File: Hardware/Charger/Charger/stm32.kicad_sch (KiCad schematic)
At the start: 48 parts, among them J5 Conn_01x04_Socket, J6 Conn_01x04, J7 Conn_02x03_Counter_Clockwise, SW1 SW_Push, SW2 SW_Push, SW3 SW_Push, SW4 SW_Push, SW5 SW_Push, SW6 SW_Push, U3 TCAN1042VDRQ1, U4 STM32G473CCTx, U5 LTV-356T, Y1 48 MHz

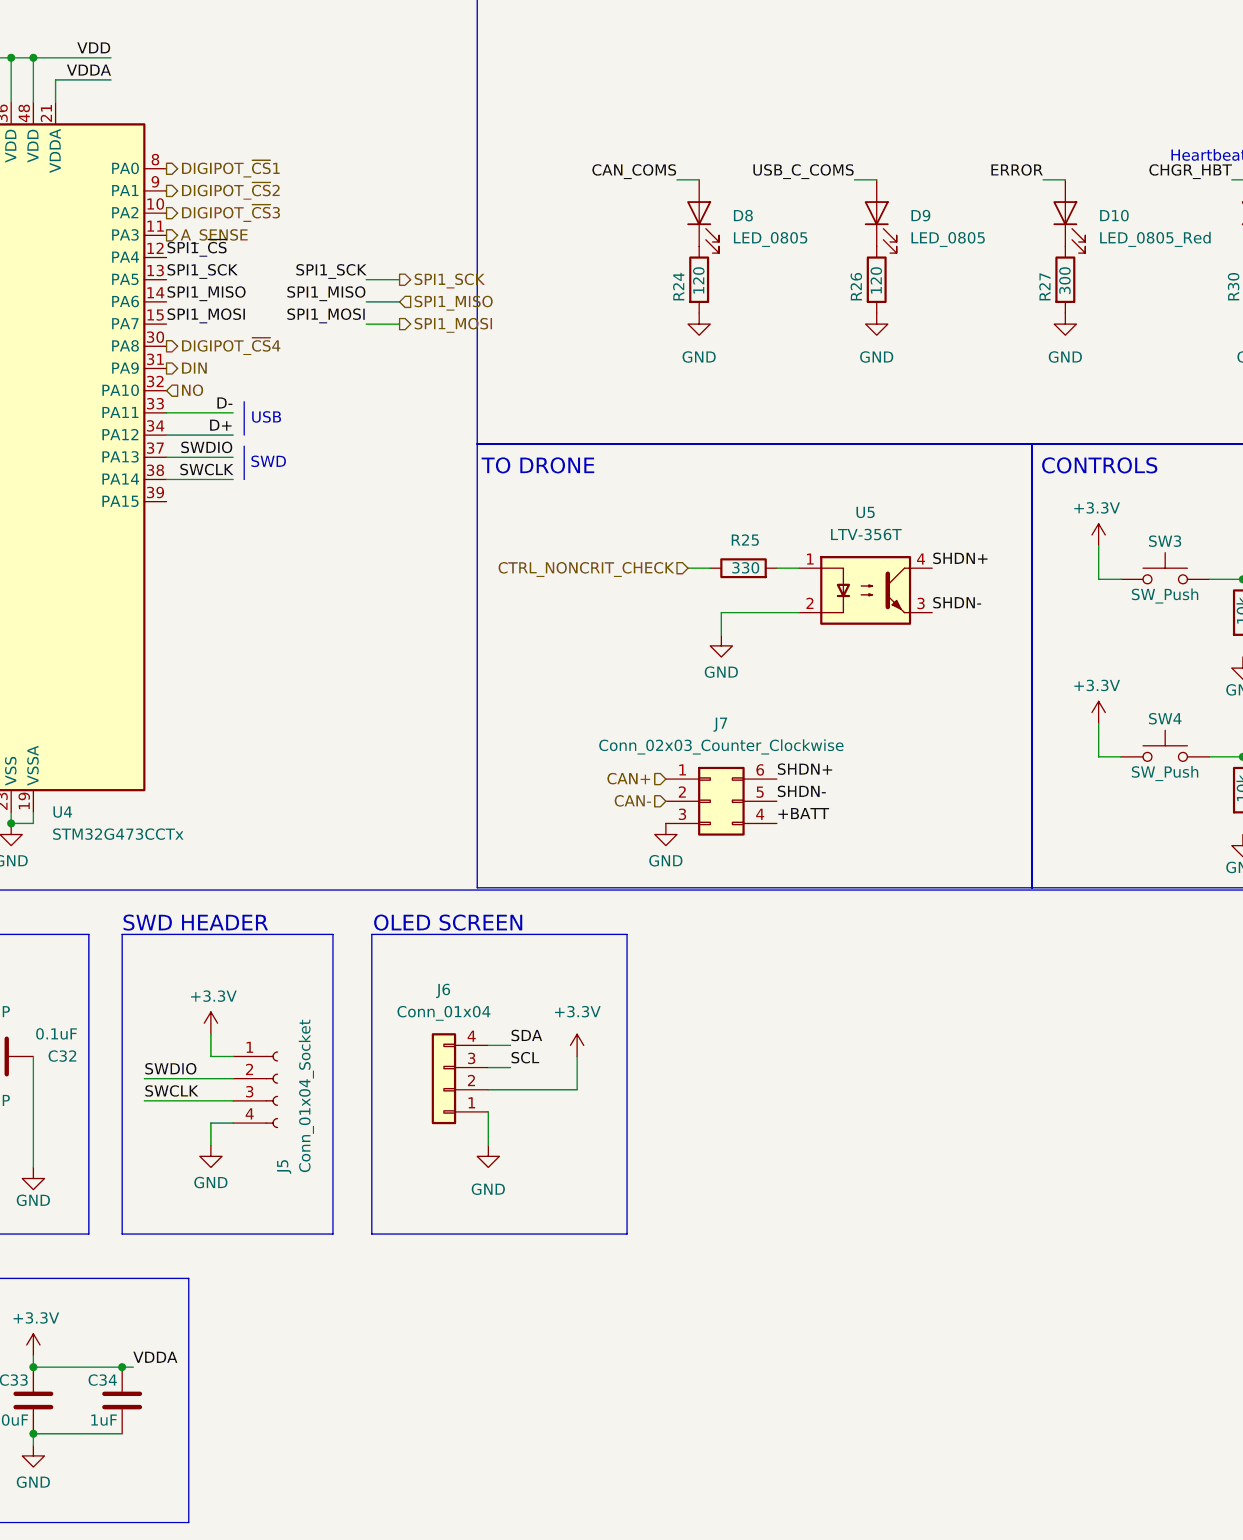
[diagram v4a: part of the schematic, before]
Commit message: edits to charger and made ground ring bodge board. Both ready for PCB fab
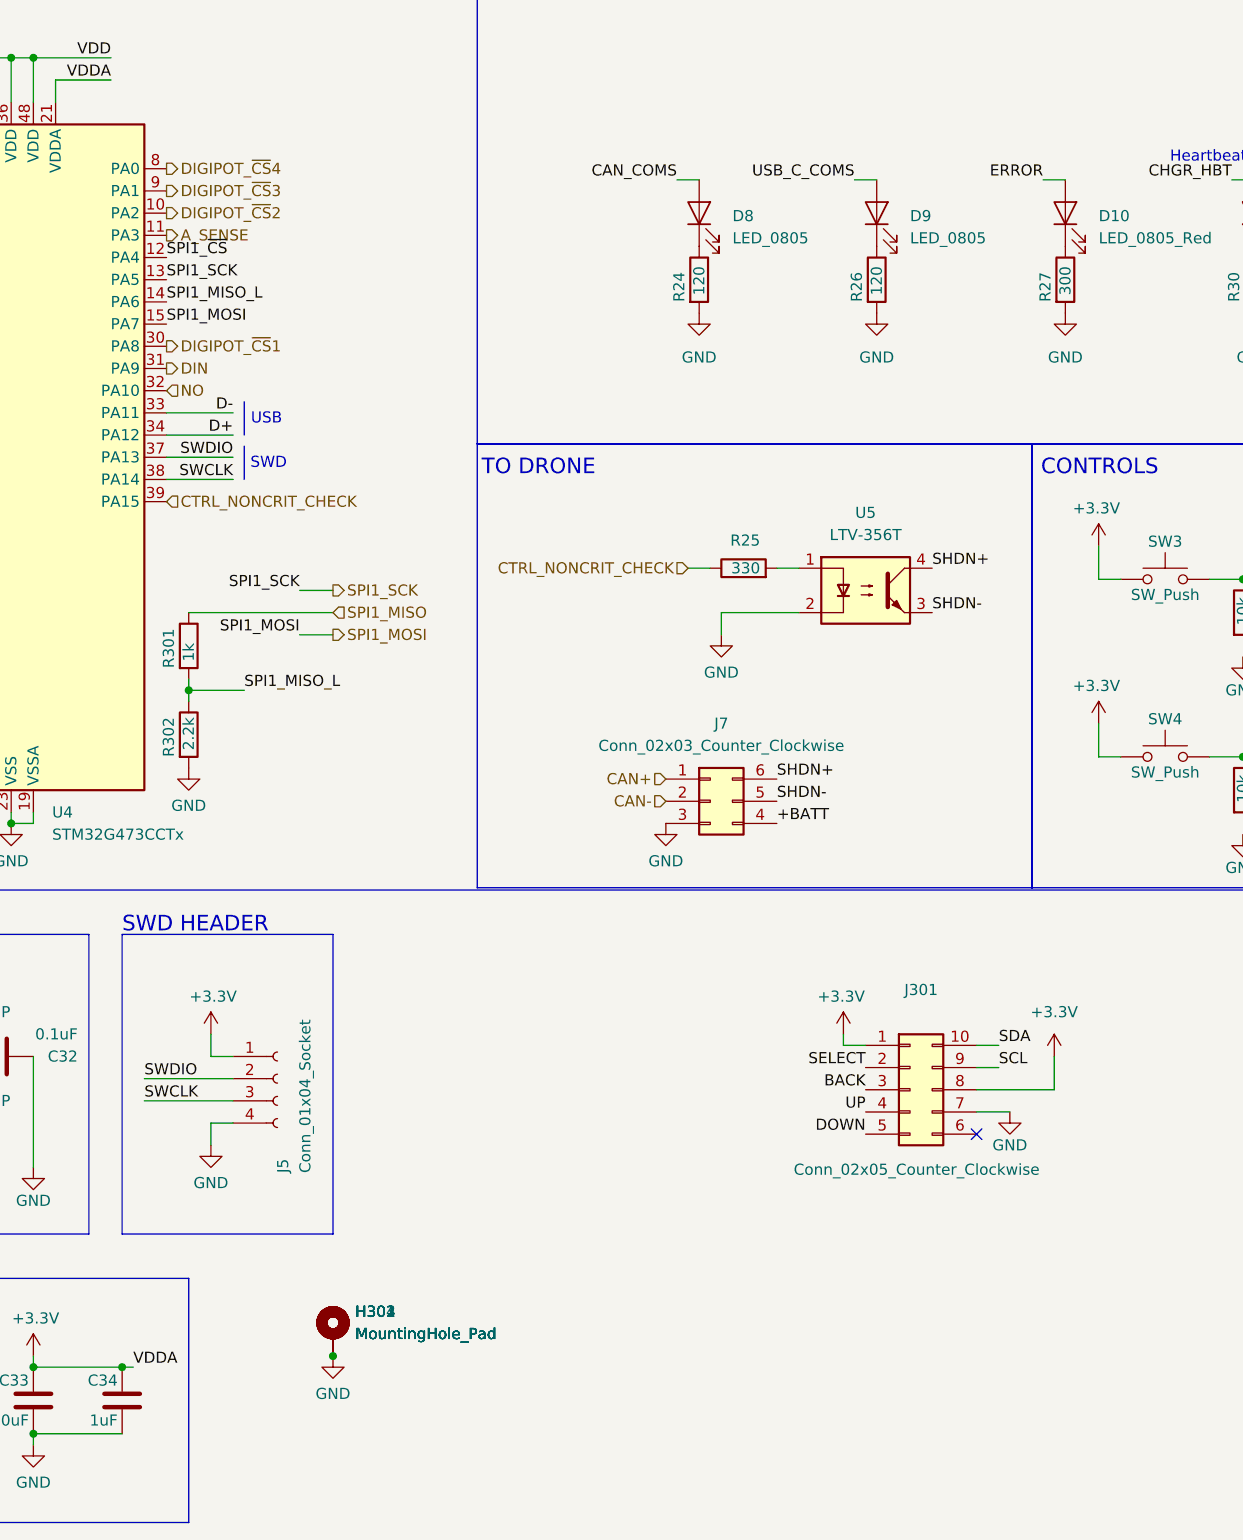
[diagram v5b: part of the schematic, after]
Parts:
- removed J6: Conn_01x04, Connector_PinHeader_2.54mm:PinHeader_1x04_P2.54mm_Vertical, symbol Connector_Generic:Conn_01x04
- added H301, H302, H303, H304: MountingHole_Pad, MountingHole:MountingHole_3.2mm_M3_Pad_Via, symbol Mechanical:MountingHole_Pad
- added J301: Conn_02x05_Counter_Clockwise, Connector_Molex:Molex_Micro-Fit_3.0_43045-1000_2x05_P3.00mm_Horizontal, symbol Connector_Generic:Conn_02x05_Counter_Clockwise
- added R301: 1k, Resistor_SMD:R_0603_1608Metric, symbol OEM:120R_DNP
- added R302: 2.2k, Resistor_SMD:R_0603_1608Metric, symbol OEM:120R_DNP
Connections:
- net +3.3V: now also J301.1 (Pin_1), J301.8 (Pin_8)
- net BACK: now also J301.3 (Pin_3)
- net CTRL_NONCRIT_CHECK: now also U4.39 (PA15)
- net DIGIPOT_~{CS}1: now also U4.30 (PA8); no longer U4.8 (PA0)
- net DIGIPOT_~{CS}2: now also U4.10 (PA2); no longer U4.9 (PA1)
- net DIGIPOT_~{CS}3: now also U4.9 (PA1); no longer U4.10 (PA2)
- net DIGIPOT_~{CS}4: now also U4.8 (PA0); no longer U4.30 (PA8)
- net DOWN: now also J301.5 (Pin_5)
- net GND: now also H301.1, H302.1, H303.1, H304.1, J301.7 (Pin_7), R302.2
- net SCL: now also J301.9 (Pin_9)
- net SDA: now also J301.10 (Pin_10)
- net SELECT: now also J301.2 (Pin_2)
- net SPI1_MISO: now also R301.1; no longer U4.14 (PA6)
- net UP: now also J301.4 (Pin_4)
- new net SPI1_MISO_L: R301.2, R302.1, U4.14 (PA6)
- no-connect marks 3 -> 4
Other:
- note removed: "OLED SCREEN"
